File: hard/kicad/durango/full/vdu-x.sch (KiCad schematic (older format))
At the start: 49 parts, among them J105 SCART, J206 VIDEO, J4 LED, Q306 BC548, Q4 BC548, Q5 BC548, U124 74HC574, U125 74HC157, U126 HC86, U127 74HC245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

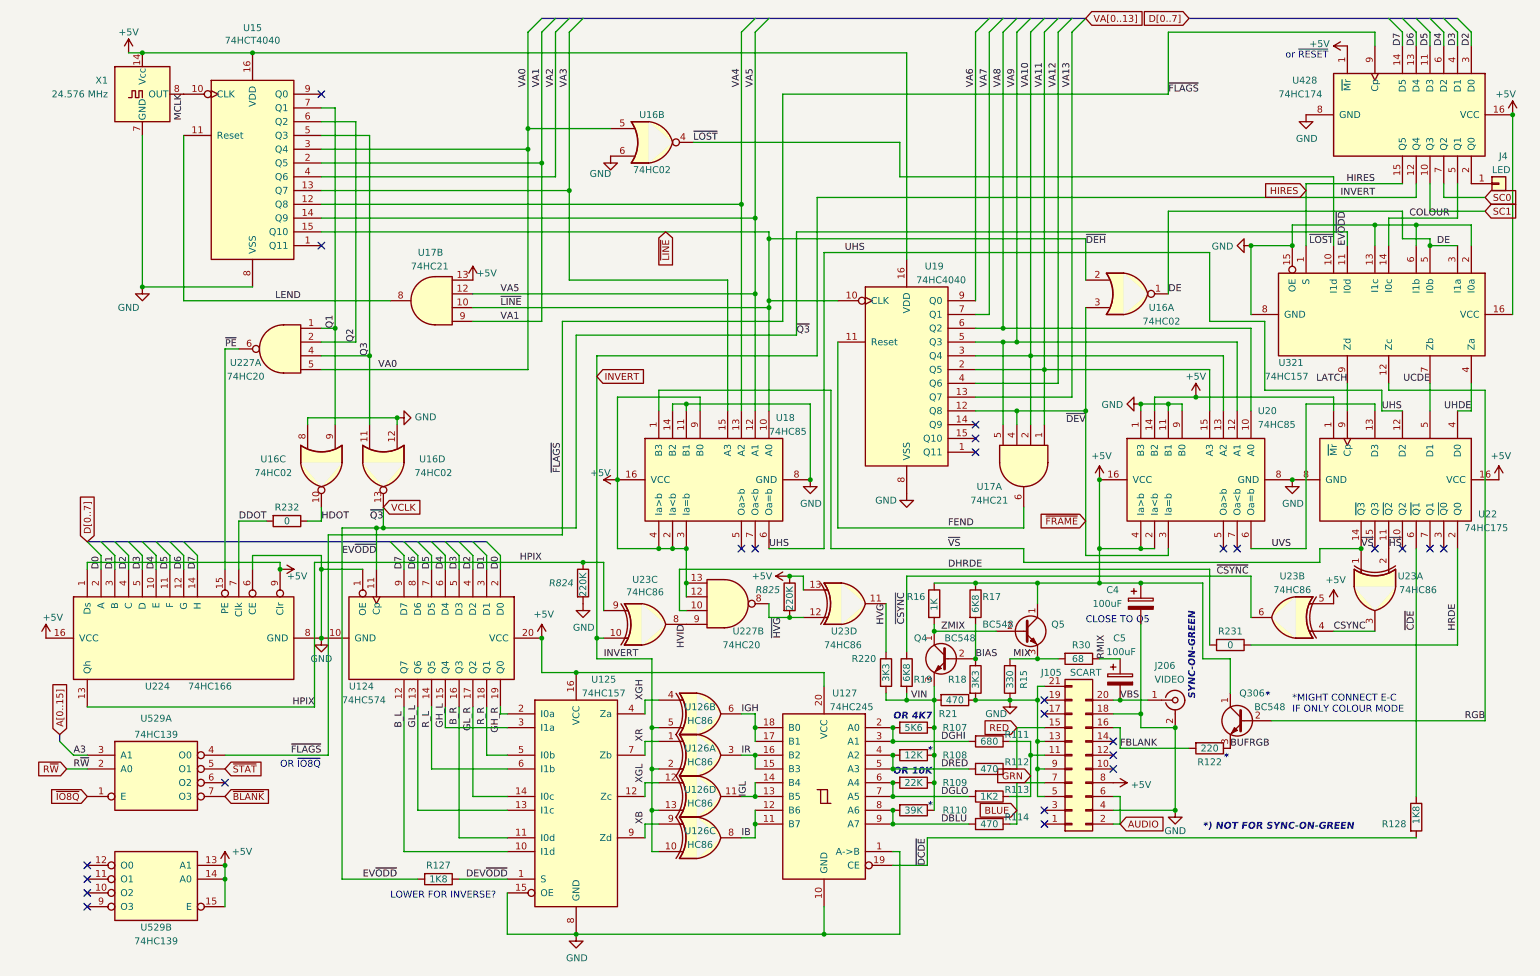
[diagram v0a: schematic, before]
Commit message: revamp SCART & colour lines
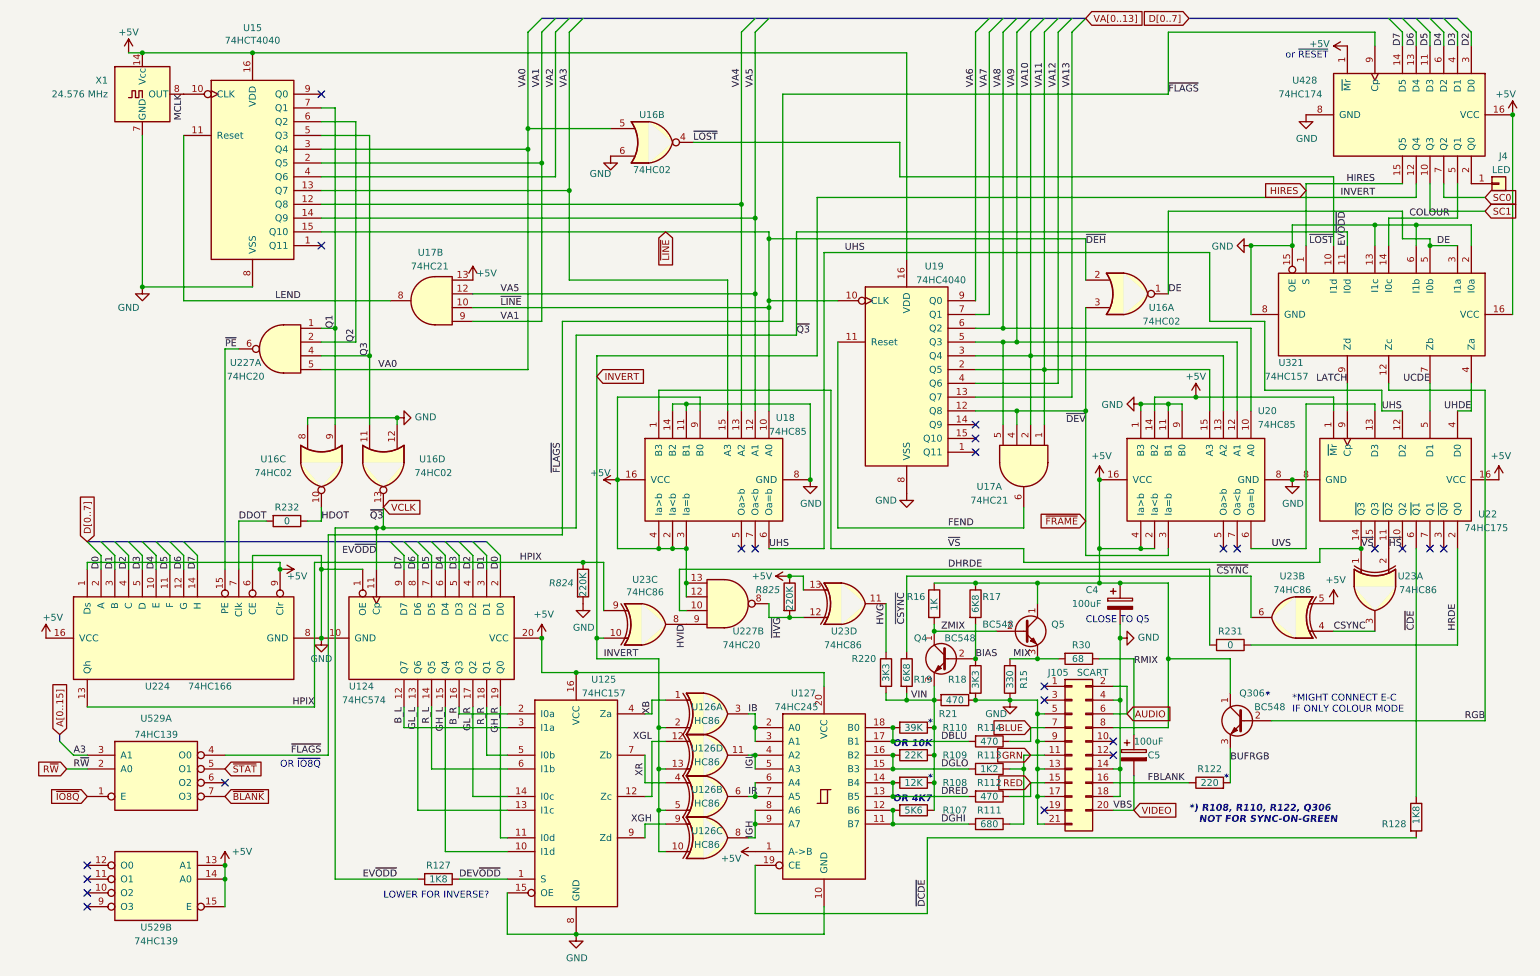
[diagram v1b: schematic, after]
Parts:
- removed J206: VIDEO, Connector_PinHeader_2.54mm:PinHeader_1x02_P2.54mm_Vertical, symbol Connector:Conn_Coaxial
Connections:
- net +5V: now also U127.1 (A->B)
- net BUFRGB: now also R122.2; no longer R122.1
- net B_L: now also U125.3 (I1a); no longer U125.10 (I1d)
- net B_R: now also U125.2 (I0a); no longer U125.11 (I0d)
- net DBLU: now also U127.17 (B1), U127.18 (B0); no longer U127.8 (A6), U127.9 (A7)
- net DGHI: now also U127.11 (B7), U127.12 (B6); no longer U127.2 (A0), U127.3 (A1)
- net DGLO: now also U127.15 (B3), U127.16 (B2); no longer U127.6 (A4), U127.7 (A5)
- net DRED: now also U127.13 (B5), U127.14 (B4); no longer U127.4 (A2), U127.5 (A3)
- net FBLANK: now also R122.1; no longer R122.2
- net GH_L: now also U125.10 (I1d); no longer U125.3 (I1a)
- net GH_R: now also U125.11 (I0d); no longer U125.2 (I0a)
- net GND: now also J105.14 (Pin_14), J105.17 (Pin_17); no longer U127.1 (A->B)
- net IB: now also U126.3, U127.2 (A0), U127.3 (A1); no longer U126.8, U127.11 (B7), U127.12 (B6)
- net IGH: now also U126.8, U127.8 (A6), U127.9 (A7); no longer U126.6, U127.17 (B1), U127.18 (B0)
- net IGL: now also U127.4 (A2), U127.5 (A3); no longer U127.13 (B5), U127.14 (B4)
- net IR: now also U126.6, U127.6 (A4), U127.7 (A5); no longer U126.3, U127.15 (B3), U127.16 (B2)
- net XB: now also U125.4 (Za), U126.1; no longer U125.9 (Zd), U126.9
- net XGH: now also U125.9 (Zd), U126.9; no longer U125.4 (Za), U126.4
- net XR: now also U126.4; no longer U126.1
- net VBS renamed VIDEO
- no-connect marks 25 -> 23
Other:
- note added: "*) R108, R110, R122, Q306\n NOT FOR SYNC-ON-GREEN"
- note removed: "*) NOT FOR SYNC-ON-GREEN"
- note removed: "SYNC-ON-GREEN"
- moved on the sheet: C4, C5, R107, R108, R109, R110, R111, R112, R113, R114, R122, U126A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

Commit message: PINOUT: video mode set and extra
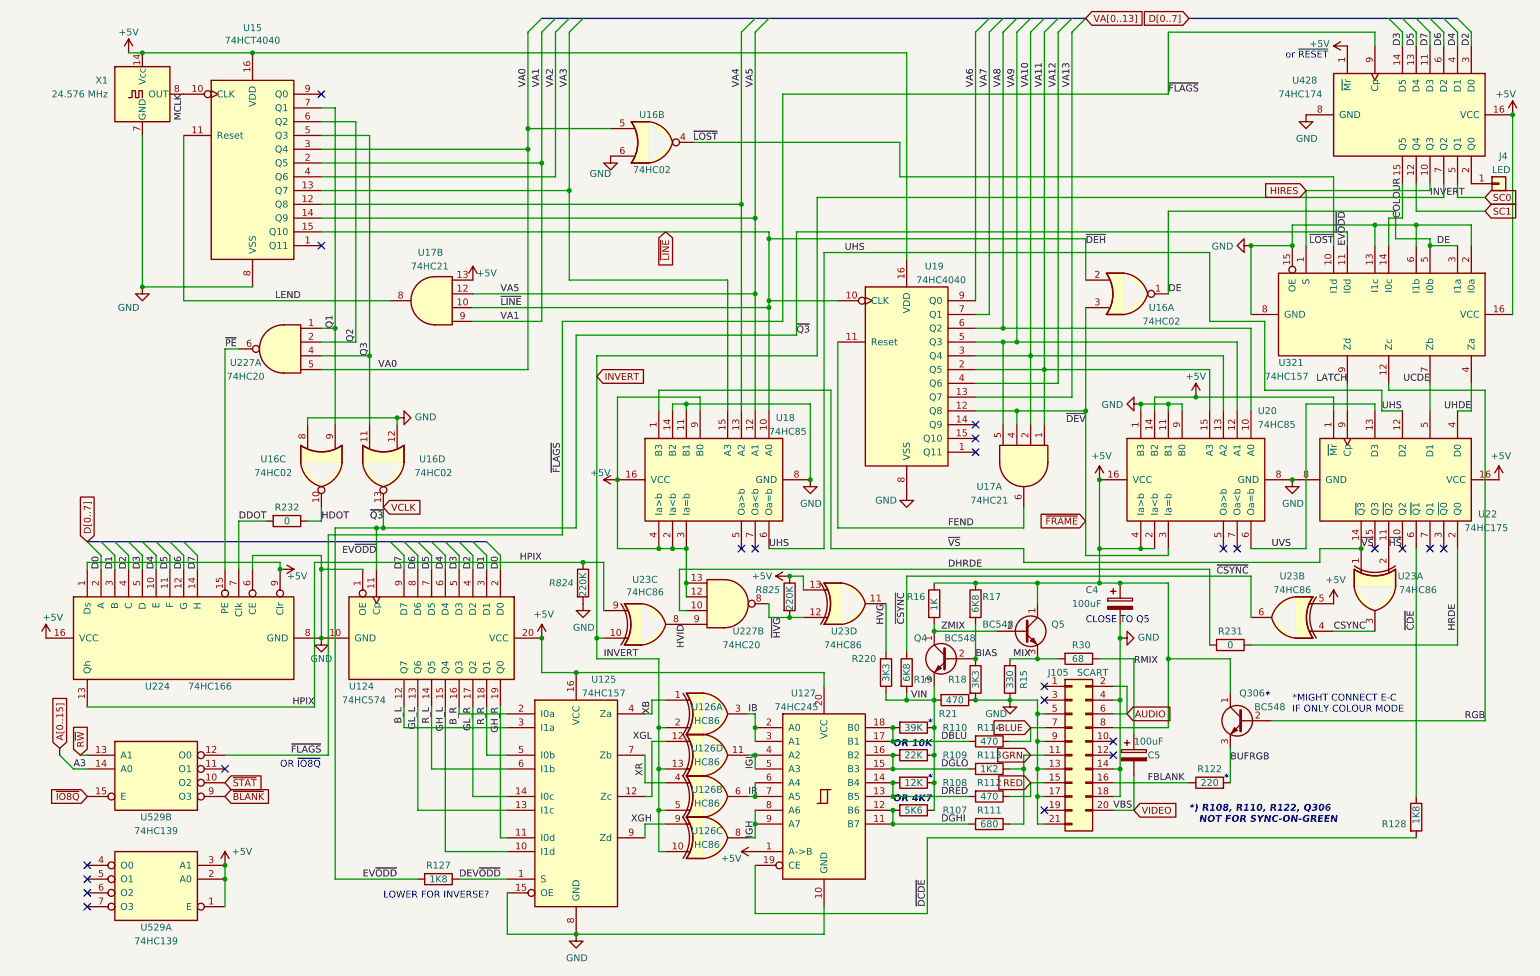
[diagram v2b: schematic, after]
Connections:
- net +5V: now also U529.1 (E), U529.2 (A0), U529.3 (A1); no longer U529.13 (A1), U529.14 (A0), U529.15 (E)
- net A3: now also U529.14 (A0); no longer U529.3 (A1)
- net COLOUR: now also U428.15 (Q5); no longer U428.5 (Q1)
- net D3: now also U428.14 (D5); no longer U428.4 (D1)
- net D4: now also U428.4 (D1); no longer U428.6 (D2)
- net D5: now also U428.13 (D4); no longer U428.11 (D3)
- net D6: now also U428.6 (D2); no longer U428.13 (D4)
- net D7: now also U428.11 (D3); no longer U428.14 (D5)
- net HIRES: now also U428.10 (Q3); no longer U428.15 (Q5)
- net INVERT: now also U428.7 (Q2); no longer U428.12 (Q4)
- net R~W: now also U529.13 (A1); no longer U529.2 (A0)
- net SC0: now also U428.5 (Q1); no longer U428.7 (Q2)
- net SC1: now also U428.12 (Q4); no longer U428.10 (Q3)
- net ~BLANK: now also U529.9 (O3); no longer U529.7 (O3)
- net ~FLAGS: now also U529.12 (O0); no longer U529.4 (O0)
- net ~IO8Q: now also U529.15 (E); no longer U529.1 (E)
- net ~STAT: now also U529.10 (O2); no longer U529.5 (O1)
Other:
- moved on the sheet: U529A, U529B
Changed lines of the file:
@@
 Entry Wire Line
 	10350 550  10450 650
-Text Label 10450 750  1    50   ~ 0
+Text Label 10650 750  1    50   ~ 0
 D6
-Text Label 10350 750  1    50   ~ 0
+Text Label 10550 750  1    50   ~ 0
 D7
 Wire Wire Line
@@
 Text Label 10850 3400 2    50   ~ 0
 UHDE
-Text Label 9900 1850 0    50   ~ 0
+Text Label 10550 1850 0    50   ~ 0
 INVERT
 Text Label 9950 3200 2    50   ~ 0
@@
 	10250 2200 10250 2000
 Wire Wire Line
-	9650 1750 9650 2200
+	9650 1800 9650 2200
 Wire Wire Line
 	9850 1700 9850 2200
@@
 	9850 1700 6700 1700
 Wire Wire Line
-	8650 1950 10350 1950
+	8650 1950 10300 1950
 Wire Wire Line
 	10550 2150 10550 2200
 Text Label 10950 5650 2    50   ~ 0
 RGB
-Text Label 10150 1750 2    50   ~ 0
-HIRES
-Wire Wire Line
-	9650 1750 10350 1750
 Wire Wire Line
 	6100 3000 6100 1850
 Wire Wire Line
-	6100 1850 10450 1850
-Wire Wire Line
-	10450 1850 10450 1750
+	6100 1850 10650 1850
 Entry Wire Line
 	10450 550  10550 650
@@
 Wire Wire Line
 	10850 650  10850 750
-Text Label 10550 750  1    50   ~ 0
+Text Label 10450 750  1    50   ~ 0
 D5
-Text Label 10650 750  1    50   ~ 0
+Text Label 10750 750  1    50   ~ 0
 D4
-Text Label 10750 750  1    50   ~ 0
+Text Label 10350 750  1    50   ~ 0
 D3
 Text Label 10850 750  1    50   ~ 0
@@
 Connection ~ 11150 1250
 Wire Wire Line
-	10550 2150 10350 2150
-Wire Wire Line
-	10350 2150 10350 1950
+	10550 2150 10300 2150
+Wire Wire Line
+	10300 2150 10300 1950
 $Comp
 L power:GND #PWR0156
@@
 L 74xx:74LS139 U?
 U 1 1 62331A7A
-P 1300 6000
+P 1300 6800
 AR Path="/6310B9C7/62331A7A" Ref="U?"  Part="1"
 AR Path="/60C42E7C/62331A7A" Ref="U529"  Part="1"
-F 0 "U529" H 1300 6367 50  0000 C CNN
-F 1 "74HC139" H 1300 6250 50  0000 C CNN
-F 2 "Package_DIP:DIP-16_W7.62mm_Socket" H 1300 6000 50  0001 C CNN
-F 3 "http://www.ti.com/lit/gpn/sn74LS139" H 1300 6000 50  0001 C CNN
-	1    1300 6000
-	1    0    0    -1
+F 0 "U529" H 1300 6450 50  0000 C CNN
+F 1 "74HC139" H 1300 6350 50  0000 C CNN
+F 2 "Package_DIP:DIP-16_W7.62mm_Socket" H 1300 6800 50  0001 C CNN
+F 3 "http://www.ti.com/lit/gpn/sn74LS139" H 1300 6800 50  0001 C CNN
+	1    1300 6800
+	-1   0    0    -1
 $EndComp
 Text GLabel 800  6200 0    50   Input ~ 0
 ~IO8Q
-NoConn ~ 1800 6100
-Entry Wire Line
-	600  5800 700  5900
-Text Label 700  5900 0    50   ~ 0
+NoConn ~ 1800 6000
+Entry Wire Line
+	600  5900 700  6000
+Text Label 700  6000 0    50   ~ 0
 A3
 Wire Wire Line
-	700  5900 800  5900
+	700  6000 800  6000
 Wire Wire Line
 	1800 5900 2550 5900
 Text Label 2500 5900 2    50   ~ 0
 ~FLAGS
-Text GLabel 1800 6000 2    50   Input ~ 0
+Text GLabel 1800 6100 2    50   Input ~ 0
 ~STAT
 Text GLabel 1800 6200 2    50   Input ~ 0
@@
 Wire Wire Line
 	3100 5550 3100 5700
-Text GLabel 600  5750 1    50   Input ~ 0
+Text GLabel 600  5850 1    50   Input ~ 0
 A[0..15]
 Connection ~ 10550 2200
@@
 	0    1    1    0
 $EndComp
-Wire Wire Line
-	650  6000 800  6000
 $Comp
 L power:+5V #PWR0113
@@
 	1    0    0    -1
 $EndComp
-Text Label 700  6000 0    50   ~ 0
-R~W
 Wire Wire Line
 	5150 4850 5100 4850
@@
 SC1
 Wire Wire Line
-	10650 1850 10650 1750
-Wire Wire Line
-	10950 1950 10550 1950
-Wire Wire Line
-	10550 1950 10550 1750
+	10950 1950 10450 1950
 Text Notes 2950 6950 0    50   ~ 0
 LOWER FOR INVERSE?
@@
 	11150 1250 11150 2700
 Wire Wire Line
-	10950 1850 10650 1850
-Wire Wire Line
-	10250 2000 10750 2000
-Wire Wire Line
-	10750 2000 10750 1750
-Text Label 10400 2000 0    50   ~ 0
+	10950 1850 10750 1850
+Wire Wire Line
+	10250 2000 10350 2000
+Text Label 10350 2000 1    50   ~ 0
 COLOUR
 $Comp
@@
 L 74xx:74LS139 U?
 U 2 1 62331A80
-P 1300 6800
+P 1300 6000
 AR Path="/6310B9C7/62331A80" Ref="U?"  Part="2"
 AR Path="/60C42E7C/62331A80" Ref="U529"  Part="2"
-F 0 "U529" H 1300 6450 50  0000 C CNN
-F 1 "74HC139" H 1300 6350 50  0000 C CNN
-F 2 "Package_DIP:DIP-16_W7.62mm_Socket" H 1300 6800 50  0001 C CNN
-F 3 "http://www.ti.com/lit/gpn/sn74LS139" H 1300 6800 50  0001 C CNN
-	2    1300 6800
-	-1   0    0    -1
+F 0 "U529" H 1300 5650 50  0000 C CNN
+F 1 "74HC139" H 1300 5550 50  0000 C CNN
+F 2 "Package_DIP:DIP-16_W7.62mm_Socket" H 1300 6000 50  0001 C CNN
+F 3 "http://www.ti.com/lit/gpn/sn74LS139" H 1300 6000 50  0001 C CNN
+	2    1300 6000
+	1    0    0    -1
 $EndComp
 Wire Wire Line
@@
 Connection ~ 1800 6700
 Wire Bus Line
-	600  5750 600  5800
-Text GLabel 650  6000 0    50   Input ~ 0
+	600  5850 600  5900
+Text GLabel 750  5900 1    50   Input ~ 0
 R~W
 Text Label 2900 4450 2    50   ~ 0
@@
 	0    -1   -1   0
 $EndComp
+Wire Wire Line
+	10650 1850 10650 1750
+Wire Wire Line
+	10450 1950 10450 1750
+Wire Wire Line
+	10750 1850 10750 1750
+Wire Wire Line
+	10350 2000 10350 1750
+Wire Wire Line
+	9650 1800 10550 1800
+Wire Wire Line
+	10550 1800 10550 1750
+Wire Wire Line
+	750  5900 800  5900
 Wire Bus Line
 	8800 550  10750 550
